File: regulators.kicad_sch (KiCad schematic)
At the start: 0 parts

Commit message: write some things down
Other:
- note added: "voltage test points"
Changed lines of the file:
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@@
     (company "Ian Kilgore")
+  )
+  (text "voltage test points" (at 38.1 31.75 0)
+    (effects (font (size 1.27 1.27)) (justify left bottom))
   )
   (symbol (lib_id "power:+5V") (at 73.66 43.18 0) (unit 1)
     (in_bom yes) (on_board yes) (fields_autoplaced)
-    (property "Reference" "#PWR?" (id 0) (at 73.66 46.99 0)
+    (property "Reference" "#PWR04" (id 0) (at 73.66 46.99 0)
       (effects (font (size 1.27 1.27)) hide)
     )
@@
   (symbol (lib_id "power:+1V35") (at 72.39 54.61 0) (unit 1)
     (in_bom yes) (on_board yes) (fields_autoplaced)
-    (property "Reference" "#PWR?" (id 0) (at 72.39 58.42 0)
+    (property "Reference" "#PWR03" (id 0) (at 72.39 58.42 0)
       (effects (font (size 1.27 1.27)) hide)
     )
@@
   (symbol (lib_id "power:GND") (at 60.96 62.23 0) (unit 1)
     (in_bom yes) (on_board yes) (fields_autoplaced)
-    (property "Reference" "#PWR?" (id 0) (at 60.96 68.58 0)
+    (property "Reference" "#PWR02" (id 0) (at 60.96 68.58 0)
       (effects (font (size 1.27 1.27)) hide)
     )
@@
   (symbol (lib_id "power:+3V3") (at 55.88 50.8 0) (unit 1)
     (in_bom yes) (on_board yes) (fields_autoplaced)
-    (property "Reference" "#PWR?" (id 0) (at 55.88 54.61 0)
+    (property "Reference" "#PWR01" (id 0) (at 55.88 54.61 0)
       (effects (font (size 1.27 1.27)) hide)
     )

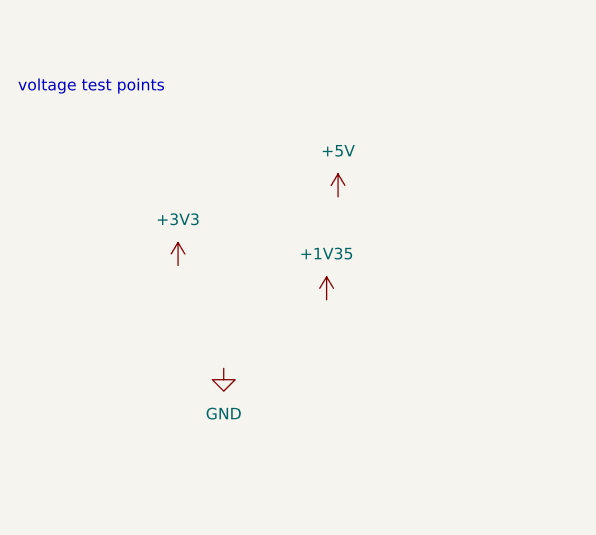
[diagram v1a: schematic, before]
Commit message: Core power; clock/ctrl
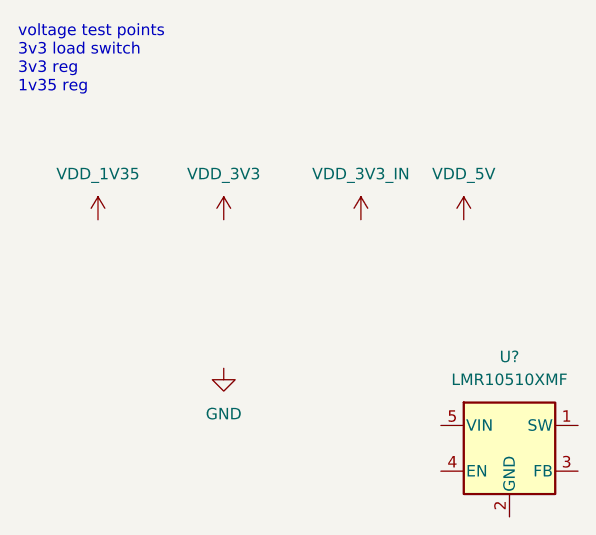
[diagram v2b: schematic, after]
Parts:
- added U?: LMR10510XMF, Package_TO_SOT_SMD:SOT-23-5, symbol Regulator_Switching:LMR10510XMF
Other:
- note added: "voltage test points 3v3 load switch 3v3 reg 1v35 reg"
- note removed: "voltage test points"
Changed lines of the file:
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@@
     (company "Ian Kilgore")
   )
-  (text "voltage test points" (at 38.1 31.75 0)
+  (text "voltage test points\n3v3 load switch\n3v3 reg\n1v35 reg"
+    (at 38.1 31.75 0)
     (effects (font (size 1.27 1.27)) (justify left bottom))
   )
-  (symbol (lib_id "power:+5V") (at 73.66 43.18 0) (unit 1)
+  (symbol (lib_id "catfood:VDD_1V35") (at 46.99 45.72 0) (unit 1)
     (in_bom yes) (on_board yes) (fields_autoplaced)
-    (property "Reference" "#PWR04" (id 0) (at 73.66 46.99 0)
+    (property "Reference" "#PWR?" (id 0) (at 46.99 49.53 0)
       (effects (font (size 1.27 1.27)) hide)
     )
-    (property "Value" "+5V" (id 1) (at 73.66 38.1 0))
-    (property "Footprint" "" (id 2) (at 73.66 43.18 0)
+    (property "Value" "VDD_1V35" (id 1) (at 46.99 40.64 0))
+    (property "Footprint" "" (id 2) (at 46.99 45.72 0)
       (effects (font (size 1.27 1.27)) hide)
     )
-    (property "Datasheet" "" (id 3) (at 73.66 43.18 0)
+    (property "Datasheet" "" (id 3) (at 46.99 45.72 0)
       (effects (font (size 1.27 1.27)) hide)
     )
     (pin "1")
   )
-  (symbol (lib_id "power:+1V35") (at 72.39 54.61 0) (unit 1)
+  (symbol (lib_id "Regulator_Switching:LMR10510XMF") (at 92.71 71.12 0) (unit 1)
     (in_bom yes) (on_board yes) (fields_autoplaced)
-    (property "Reference" "#PWR03" (id 0) (at 72.39 58.42 0)
+    (property "Reference" "U?" (id 0) (at 92.71 60.96 0))
+    (property "Value" "LMR10510XMF" (id 1) (at 92.71 63.5 0))
+    (property "Footprint" "Package_TO_SOT_SMD:SOT-23-5" (id 2) (at 93.98 77.47 0)
+      (effects (font (size 1.27 1.27) italic) (justify left) hide)
+    )
+    (property "Datasheet" "http://www.ti.com/lit/ds/symlink/lmr10510.pdf" (id 3) (at 92.71 68.58 0)
       (effects (font (size 1.27 1.27)) hide)
     )
-    (property "Value" "+1V35" (id 1) (at 72.39 49.53 0))
-    (property "Footprint" "" (id 2) (at 72.39 54.61 0)
+    (pin "1")
+    (pin "2")
+    (pin "3")
+    (pin "4")
+    (pin "5")
+  )
+  (symbol (lib_id "catfood:VDD_3V3") (at 60.96 45.72 0) (unit 1)
+    (in_bom yes) (on_board yes) (fields_autoplaced)
+    (property "Reference" "#PWR?" (id 0) (at 60.96 49.53 0)
       (effects (font (size 1.27 1.27)) hide)
     )
-    (property "Datasheet" "" (id 3) (at 72.39 54.61 0)
+    (property "Value" "VDD_3V3" (id 1) (at 60.96 40.64 0))
+    (property "Footprint" "" (id 2) (at 60.96 45.72 0)
+      (effects (font (size 1.27 1.27)) hide)
+    )
+    (property "Datasheet" "" (id 3) (at 60.96 45.72 0)
+      (effects (font (size 1.27 1.27)) hide)
+    )
+    (pin "1")
+  )
+  (symbol (lib_id "catfood:VDD_3V3_IN") (at 76.2 45.72 0) (unit 1)
+    (in_bom yes) (on_board yes) (fields_autoplaced)
+    (property "Reference" "#PWR?" (id 0) (at 76.2 49.53 0)
+      (effects (font (size 1.27 1.27)) hide)
+    )
+    (property "Value" "VDD_3V3_IN" (id 1) (at 76.2 40.64 0))
+    (property "Footprint" "" (id 2) (at 76.2 45.72 0)
+      (effects (font (size 1.27 1.27)) hide)
+    )
+    (property "Datasheet" "" (id 3) (at 76.2 45.72 0)
       (effects (font (size 1.27 1.27)) hide)
     )
@@
     (pin "1")
   )
-  (symbol (lib_id "power:+3V3") (at 55.88 50.8 0) (unit 1)
+  (symbol (lib_id "catfood:VDD_5V") (at 87.63 45.72 0) (unit 1)
     (in_bom yes) (on_board yes) (fields_autoplaced)
-    (property "Reference" "#PWR01" (id 0) (at 55.88 54.61 0)
+    (property "Reference" "#PWR?" (id 0) (at 87.63 49.53 0)
       (effects (font (size 1.27 1.27)) hide)
     )
-    (property "Value" "+3V3" (id 1) (at 55.88 45.72 0))
-    (property "Footprint" "" (id 2) (at 55.88 50.8 0)
+    (property "Value" "VDD_5V" (id 1) (at 87.63 40.64 0))
+    (property "Footprint" "" (id 2) (at 87.63 45.72 0)
       (effects (font (size 1.27 1.27)) hide)
     )
-    (property "Datasheet" "" (id 3) (at 55.88 50.8 0)
+    (property "Datasheet" "" (id 3) (at 87.63 45.72 0)
       (effects (font (size 1.27 1.27)) hide)
     )

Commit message: Regulators
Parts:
- added C? (x3): 0.1uF 0402, symbol Device:C_Small
- added C? (x6): 10uF 0805, symbol Device:C_Small
- added C?: 1uF 0402, symbol Device:C_Small
- added C?: DNI 0402, symbol Device:C_Small
- added C?: 0.22uF 0402, symbol Device:C_Small
- added C? (x2): 22uF 0805, symbol Device:C_Small
- added D?: SS14FL, symbol Device:D_Schottky
- added L?: 3.9uH, symbol Device:L_Small
- added L?: 1uH, symbol Device:L_Small
- added R?: 44.2k 0402 1%, symbol Device:R_Small
- added R?: 200k 0603 1%, symbol Device:R_Small
- added R? (x2): 100k 0402, symbol Device:R_Small
- added R?: 10k 0402 1%, symbol Device:R_Small
- added R?: 12.4k 0402 1%, symbol Device:R_Small
- added R?: 10k 0402, symbol Device:R_Small
- added R?: 3.4k 0402 1%, symbol Device:R_Small
- added TP? (x5): TestPoint, symbol Connector:TestPoint
- added U?: AP22615AWU-7, symbol catfood:AP22615AWU-7
- added U?: MP2143DJ, symbol catfood:MP2143DJ
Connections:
- net GND: now also U?.2 (GND), C?.2, C?.2, C?.2, C?.2, C?.2, C?.2, C?.2, C?.2, C?.2, C?.2, C?.2, C?.2, C?.2, C?.2, D?.2 (A), R?.2, R?.2, R?.2, TP?.1, U?.2 (GND), U?.4 (PGND), U?.6 (AGND)
- net VDD_1V35: now also C?.1, L?.2, R?.1, TP?.1
- net VDD_3V3: now also U?.5 (VIN), C?.1, C?.1, C?.1, C?.1, R?.1, TP?.1, U?. (VOUT)
- net VDD_3V3_IN: now also C?.1, C?.1, C?.1, C?.1, L?.2, R?.1, TP?.1, U?.5 (OUT), U?.6 (VIN)
- net VDD_5V: now also C?.1, C?.1, C?.1, R?.1, TP?.1, U?.2 (VIN)
- net at U?.1 (SW): now also D?.1 (K), L?.1
- net at U?.3 (FB): now also R?.1, R?.2
- net at U?.4 (EN): now also C?.1, R?.2
- new net: R?.1, R?.2, U?.7 (FB)
- new net: C?.1, R?.2, U?.4 (EN)
- new net: R?.1, U?.5 (ISET)
- new net: L?.1, U?.3 (SW)
- new net: R?.2, U?.8 (EN)
- new net PMIC_ON_REQ: R?.1
- no-connect marks 0 -> 2
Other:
- note added: "I_{lim} = 2A"
- note added: "I_{max} = 1A"
- note added: "I_{max} = 3A"
- note removed: "voltage test points 3v3 load switch 3v3 reg 1v35 reg"
- moved on the sheet: U?

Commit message: Annotation
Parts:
- gave numbers to parts that had none: 33
